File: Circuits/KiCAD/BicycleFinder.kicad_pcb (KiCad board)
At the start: 2 copper layers, 76.4 x 40.2 mm, 11 parts, among them P1 CONN_14, P2 CONN_14, P3 CONN_7, SW1 SW_PUSH, U1 LITE_LITE

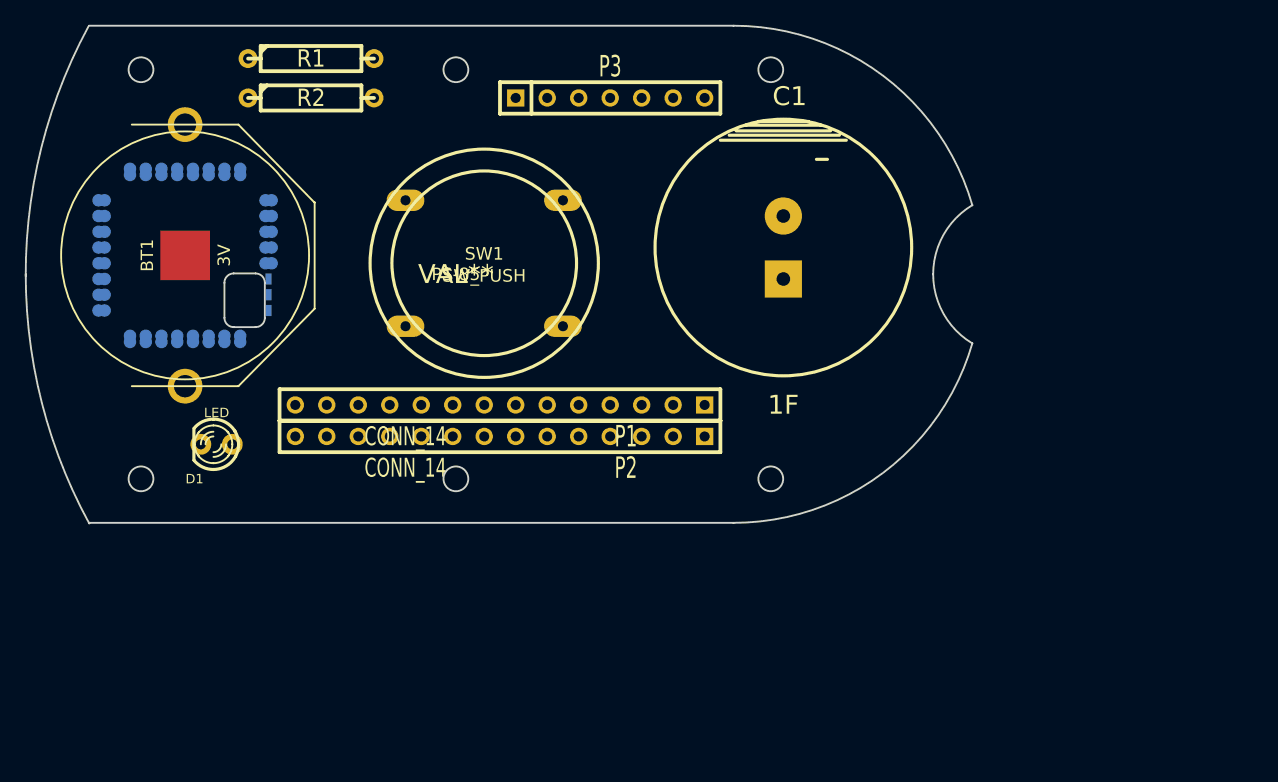
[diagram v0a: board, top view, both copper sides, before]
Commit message: Colored 1F EDLC.
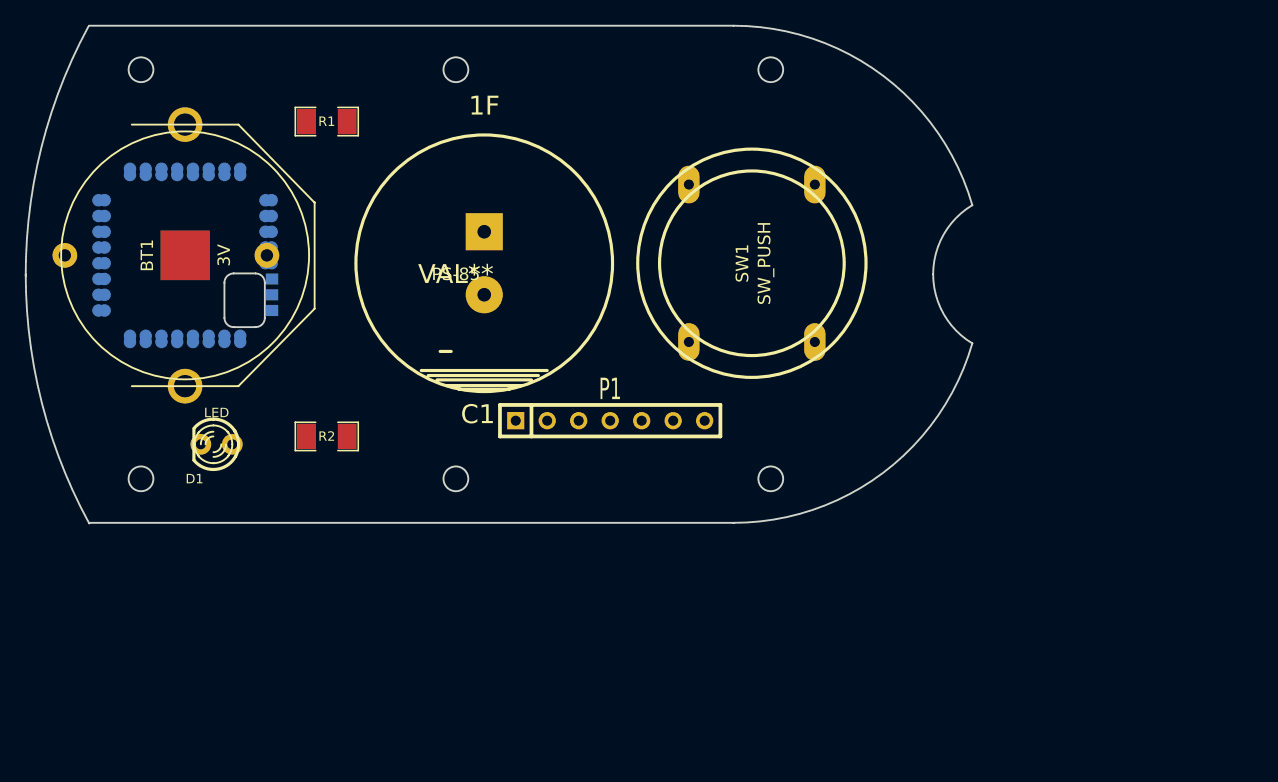
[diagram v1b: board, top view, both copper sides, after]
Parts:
- removed P2: CONN_14, SIL-14
- removed P3: CONN_7, SIL-7
- BT1: footprint BK-888 -> BK-888+BK-2032M
- P1: value CONN_14 -> CONN_7; footprint SIL-14 -> SIL-7
- R1, R2: value 1k -> 750; footprint R4 -> SM1206
- moved R2 27.3 mm to (36.8, 45.7)
- moved C1 24.2 mm to (49.5, 31.8), turned to 180 degrees
- moved SW1 21.6 mm to (71.1, 31.8), turned to 90 degrees
- moved P1 8.98 mm to (59.7, 44.5), turned to 0 degrees
- moved R1 5.24 mm to (36.8, 20.3)
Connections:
- C1 pad 1: /Vcc -> N-0000034
- D1 pad 2: /DO4 -> N-0000033
- P1 pad 1: GND -> N-0000034
- P1 pad 2: /SCL -> N-0000028
- P1 pad 3: /TXD -> N-0000029
- P1 pad 4: /PWM1 -> N-0000016
- P1 pad 5: /DO1 -> N-0000019
- P1 pad 6: /PWM2 -> N-0000028
- P1 pad 7: /PWM3 -> N-0000018
- R1 pad 2: /Vcc -> N-0000034
- R2 pad 2: /Vcc -> N-0000034
- SW1 pad 1: GND -> N-0000030
- SW1 pad 2: /DI1 -> GND
- U1 pad 1: /PWM2 -> (no net)
- U1 pad 10: /PWM4 -> (no net)
- U1 pad 11: /DO4 -> N-0000033
- U1 pad 12: /M1 -> N-0000018
- U1 pad 13: /DI1 -> N-0000030
- U1 pad 14: /SCL -> (no net)
- U1 pad 15: /DI2 -> (no net)
- U1 pad 16: /DI3 -> (no net)
- U1 pad 17: /SDA -> (no net)
- U1 pad 18: /DI4 -> (no net)
- U1 pad 19: /BPS -> (no net)
- U1 pad 2: /PWM3 -> N-0000016
- U1 pad 21: /RST -> N-0000028
- U1 pad 22: /AI3 -> (no net)
- U1 pad 23: /AI1 -> (no net)
- U1 pad 24: /AI2 -> (no net)
- U1 pad 25: /AI4 -> (no net)
- U1 pad 26: /M2 -> (no net)
- U1 pad 27: /M3 -> (no net)
- U1 pad 28: GND -> (no net)
- U1 pad 3: /DO1 -> (no net)
- U1 pad 4: /DO2 -> (no net)
- U1 pad 5: /Vcc -> N-0000034
- U1 pad 6: /DO3 -> (no net)
- U1 pad 7: /PWM1 -> (no net)
- U1 pad 8: /RXD -> N-0000029
- U1 pad 9: /TXD -> N-0000019

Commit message: Added 3D model of BK-888, BK-2032M, CR2032.
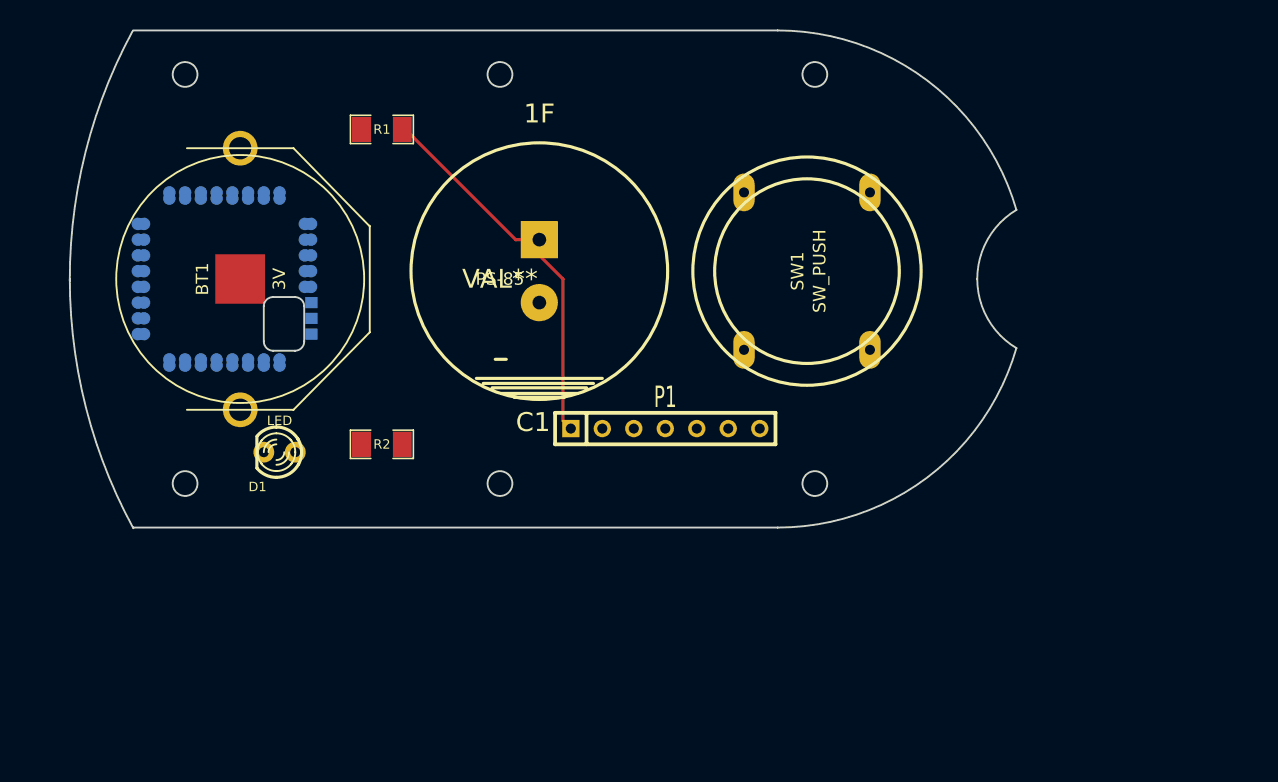
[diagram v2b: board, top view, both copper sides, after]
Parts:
- BT1: footprint BK-888+BK-2032M -> BK-888+CR2032
- moved D1 5.12 mm to (33.0, 47.0)
- moved BT1 4.84 mm to (29.8, 33.0)
- moved P1 4.49 mm to (64.1, 45.1)
- moved C1 4.49 mm to (54.0, 32.4)
- moved R1 4.49 mm to (41.3, 21.0)
- moved R2 4.49 mm to (41.3, 46.4)
- moved SW1 4.49 mm to (75.6, 32.4)
- moved U1 3.70 mm to (21.6, 40.0)
- moved PS-85 3.58 mm to (50.8, 33.0)
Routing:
- net N-0000034: track 0.00 -> 31.5 mm
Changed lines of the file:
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@@
 (kicad_pcb (version 3) (host pcbnew "(2013-07-07 BZR 4022)-stable")
   (general
-    (links 20)
-    (no_connects 20)
-    (area 12.214999 12.259999 92.573001 53.073059)
+    (links 18)
+    (no_connects 16)
+    (area 12.065 12.065 92.71 53.34)
     (thickness 1.6)
     (drawings 0)
-    (tracks 0)
+    (tracks 9)
     (zones 0)
     (modules 9)
@@
   )
   (module SW_PUSH-18mm   placed (layer F.Cu)
-    (at 71.12 31.75 90)
+    (at 75.565 32.385 90)
     (fp_text reference SW1 (at 0 -0.762 90) (layer F.SilkS)
       (effects (font (size 1.016 1.016) (thickness 0.2032)))
@@
   )
   (module LED-3MM (layer F.Cu)
-    (at 27.94 46.355 180)
+    (at 33.02 46.99 180)
     (descr "LED 3mm - Lead pitch 100mil (2,54mm)")
     (tags "LED led 3mm 3MM 100mil 2,54mm")
@@
   )
   (module PS-85 (layer F.Cu)
-    (at 47.244 32.639)
+    (at 50.8 33.02)
     (fp_text reference PS-85 (at 0 0) (layer F.SilkS)
       (effects (font (size 1 1) (thickness 0.15)))
@@
   )
   (module SE-5R5-D105VY   placed (layer F.Cu)
-    (at 49.53 31.75 180)
+    (at 53.975 32.385 180)
     (descr "Capacitor, EDLC, cyl 20.7x7.5mm")
     (fp_text reference C1 (at 0.508 -12.192 180) (layer F.SilkS)
@@
   )
   (module LITE (layer B.Cu)
-    (at 18.415 38.1 90)
+    (at 21.59 40.005 90)
     (fp_text reference U1 (at 0 0 90) (layer B.SilkS) hide
       (effects (font (size 0 0) (thickness 0.000001)) (justify mirror))
@@
   )
   (module SM1206 (layer F.Cu)
-    (at 36.83 20.32)
+    (at 41.275 20.955)
     (attr smd)
     (fp_text reference R1 (at 0 0) (layer F.SilkS)
@@
   )
   (module SM1206 (layer F.Cu)
-    (at 36.83 45.72)
+    (at 41.275 46.355)
     (attr smd)
     (fp_text reference R2 (at 0 0) (layer F.SilkS)
@@
   )
   (module SIL-7 (layer F.Cu)
-    (at 59.69 44.45)
+    (at 64.135 45.085)
     (descr "Connecteur 7 pins")
     (tags "CONN DEV")
@@
     )
   )
-  (module BK-888+BK-2032M (layer F.Cu)
-    (at 25.4 31.115 90)
+  (module BK-888+CR2032 (layer F.Cu)
+    (at 29.845 33.02 90)
     (fp_text reference BT1 (at 0 -3.05 90) (layer F.SilkS)
       (effects (font (size 1 1) (thickness 0.15)))
@@
     (fp_circle (center 0 0) (end 0 -10) (layer F.SilkS) (width 0.15))
     (pad 1 thru_hole circle (at -10.55 0 90) (size 2.8 2.8) (drill 1.8)
-      (layers *.Cu *.Mask F.SilkS)
+      (layers *.Mask B.Cu F.SilkS)
       (net 1 /3V)
     )
     (pad 1 thru_hole circle (at 10.55 0 90) (size 2.8 2.8) (drill 1.8)
-      (layers *.Cu *.Mask F.SilkS)
+      (layers *.Mask B.Cu F.SilkS)
       (net 1 /3V)
-    )
-    (pad 2 thru_hole circle (at 0 -9.7 90) (size 2 2) (drill 1)
-      (layers *.Cu *.Mask F.SilkS)
-      (net 2 GND)
-    )
-    (pad 2 thru_hole circle (at 0 6.6 90) (size 2 2) (drill 1)
-      (layers *.Cu *.Mask F.SilkS)
-      (net 2 GND)
     )
     (pad 2 smd rect (at 0 0 90) (size 4 4)
@@
       (net 2 GND)
     )
-  )
+    (model BK-888.wrl
+      (at (xyz 0 0 0))
+      (scale (xyz 0.393701 0.393701 0.393701))
+      (rotate (xyz 0 0 0))
+    )
+    (model CR2032.wrl
+      (at (xyz 0 0 0.009842999999999999))
+      (scale (xyz 0.393701 0.393701 0.393701))
+      (rotate (xyz 0 0 0))
+    )
+  )
+  (segment (start 42.926 46.355) (end 43.18 46.355) (width 0.254) (layer F.Cu) (net 11) (status 80000))
+  (segment (start 43.18 46.355) (end 42.926 46.355) (width 0.254) (layer F.Cu) (net 11) (status 80000))
+  (segment (start 53.975 29.845) (end 52.07 29.845) (width 0.254) (layer F.Cu) (net 11) (status 80000))
+  (segment (start 52.07 29.845) (end 43.18 20.955) (width 0.254) (layer F.Cu) (net 11) (status 80000))
+  (segment (start 43.18 20.955) (end 42.926 20.955) (width 0.254) (layer F.Cu) (net 11) (status 80000))
+  (segment (start 56.515 45.085) (end 55.88 44.45) (width 0.254) (layer F.Cu) (net 11) (status 80000))
+  (segment (start 55.88 44.45) (end 55.88 33.02) (width 0.254) (layer F.Cu) (net 11) (status 80000))
+  (segment (start 55.88 33.02) (end 53.975 31.115) (width 0.254) (layer F.Cu) (net 11) (status 80000))
+  (segment (start 53.975 31.115) (end 53.975 29.845) (width 0.254) (layer F.Cu) (net 11) (status 80000))
+  (zone (net 0) (net_name "") (layer F.Cu) (hatch edge 0.508)
+    (connect_pads (clearance 0.508))
+    (min_thickness 0.254)
+    (keepout (tracks not_allowed) (vias not_allowed) (copperpour allowed))
+    (fill (arc_segments 16) (thermal_gap 0.508) (thermal_bridge_width 0.508))
+    (polygon
+      (pts
+        (xy 35.56 40.005) (xy 21.59 40.005) (xy 21.59 26.035) (xy 35.56 26.035)
+      )
+    )
+  )

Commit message: Marked plus sign on BK-888 3D model.
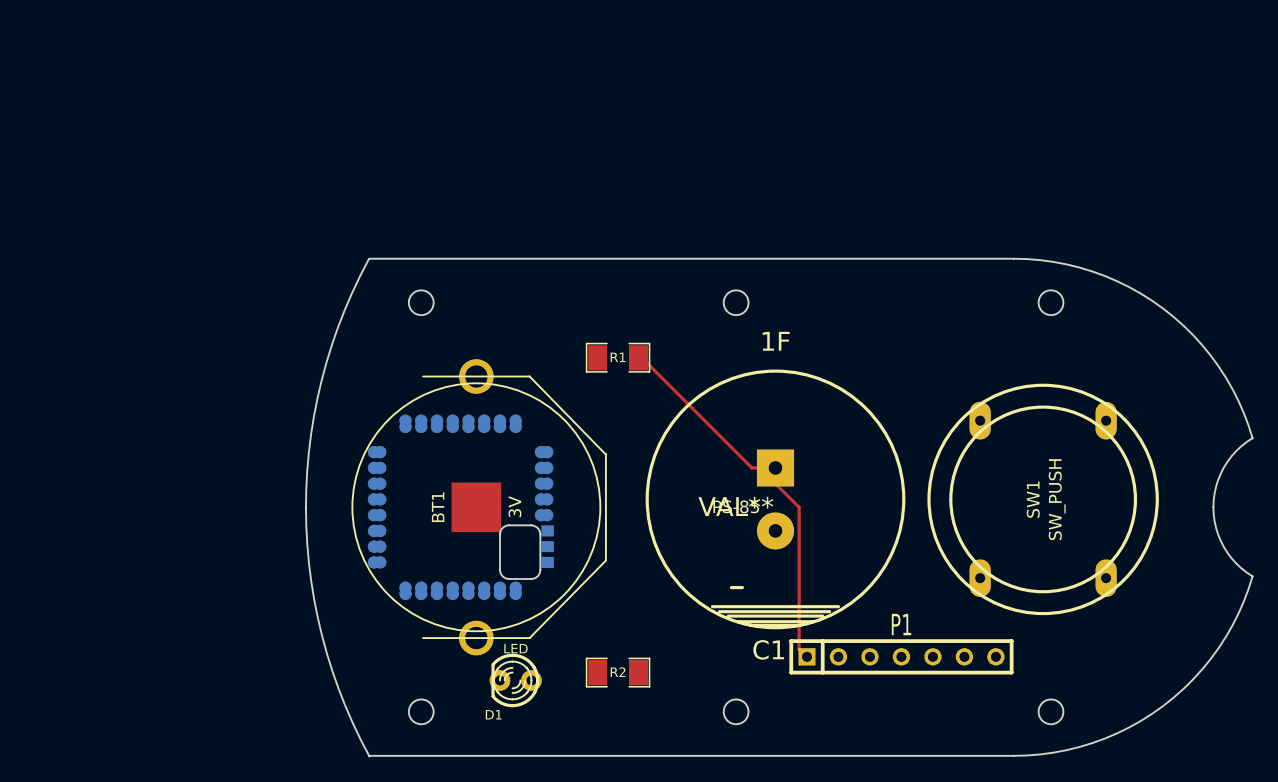
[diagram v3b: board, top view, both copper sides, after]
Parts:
- moved BT1 26.5 mm to (48.9, 51.4)
- moved C1 26.5 mm to (73.0, 50.8)
- moved R1 26.5 mm to (60.3, 39.4)
- moved R2 26.5 mm to (60.3, 64.8)
- moved D1 26.5 mm to (52.1, 65.4)
- moved P1 26.5 mm to (83.2, 63.5)
- moved PS-85 26.5 mm to (69.8, 51.4)
- moved SW1 26.5 mm to (94.6, 50.8)
- moved U1 26.5 mm to (40.6, 58.4)
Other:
- outline, holes or cut-outs redrawn
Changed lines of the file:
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@@
     (links 18)
     (no_connects 16)
-    (area 12.065 12.065 92.71 53.34)
+    (area 34.820999 31.055999 115.179001 71.869059)
     (thickness 1.6)
     (drawings 0)
@@
   )
   (module SW_PUSH-18mm   placed (layer F.Cu)
-    (at 75.565 32.385 90)
+    (at 94.615 50.8 90)
     (fp_text reference SW1 (at 0 -0.762 90) (layer F.SilkS)
       (effects (font (size 1.016 1.016) (thickness 0.2032)))
@@
   )
   (module LED-3MM (layer F.Cu)
-    (at 33.02 46.99 180)
+    (at 52.07 65.405 180)
     (descr "LED 3mm - Lead pitch 100mil (2,54mm)")
     (tags "LED led 3mm 3MM 100mil 2,54mm")
@@
   )
   (module PS-85 (layer F.Cu)
-    (at 50.8 33.02)
+    (at 69.85 51.435)
     (fp_text reference PS-85 (at 0 0) (layer F.SilkS)
       (effects (font (size 1 1) (thickness 0.15)))
@@
   )
   (module SE-5R5-D105VY   placed (layer F.Cu)
-    (at 53.975 32.385 180)
+    (at 73.025 50.8 180)
     (descr "Capacitor, EDLC, cyl 20.7x7.5mm")
     (fp_text reference C1 (at 0.508 -12.192 180) (layer F.SilkS)
@@
   )
   (module LITE (layer B.Cu)
-    (at 21.59 40.005 90)
+    (at 40.64 58.42 90)
     (fp_text reference U1 (at 0 0 90) (layer B.SilkS) hide
       (effects (font (size 0 0) (thickness 0.000001)) (justify mirror))
@@
   )
   (module SM1206 (layer F.Cu)
-    (at 41.275 20.955)
+    (at 60.325 39.37)
     (attr smd)
     (fp_text reference R1 (at 0 0) (layer F.SilkS)
@@
   )
   (module SM1206 (layer F.Cu)
-    (at 41.275 46.355)
+    (at 60.325 64.77)
     (attr smd)
     (fp_text reference R2 (at 0 0) (layer F.SilkS)
@@
   )
   (module SIL-7 (layer F.Cu)
-    (at 64.135 45.085)
+    (at 83.185 63.5)
     (descr "Connecteur 7 pins")
     (tags "CONN DEV")
@@
   )
   (module BK-888+CR2032 (layer F.Cu)
-    (at 29.845 33.02 90)
+    (at 48.895 51.435 90)
     (fp_text reference BT1 (at 0 -3.05 90) (layer F.SilkS)
       (effects (font (size 1 1) (thickness 0.15)))
@@
     )
   )
-  (segment (start 42.926 46.355) (end 43.18 46.355) (width 0.254) (layer F.Cu) (net 11) (status 80000))
-  (segment (start 43.18 46.355) (end 42.926 46.355) (width 0.254) (layer F.Cu) (net 11) (status 80000))
-  (segment (start 53.975 29.845) (end 52.07 29.845) (width 0.254) (layer F.Cu) (net 11) (status 80000))
-  (segment (start 52.07 29.845) (end 43.18 20.955) (width 0.254) (layer F.Cu) (net 11) (status 80000))
-  (segment (start 43.18 20.955) (end 42.926 20.955) (width 0.254) (layer F.Cu) (net 11) (status 80000))
-  (segment (start 56.515 45.085) (end 55.88 44.45) (width 0.254) (layer F.Cu) (net 11) (status 80000))
-  (segment (start 55.88 44.45) (end 55.88 33.02) (width 0.254) (layer F.Cu) (net 11) (status 80000))
-  (segment (start 55.88 33.02) (end 53.975 31.115) (width 0.254) (layer F.Cu) (net 11) (status 80000))
-  (segment (start 53.975 31.115) (end 53.975 29.845) (width 0.254) (layer F.Cu) (net 11) (status 80000))
+  (segment (start 61.976 64.77) (end 62.23 64.77) (width 0.254) (layer F.Cu) (net 11) (status 80000))
+  (segment (start 62.23 64.77) (end 61.976 64.77) (width 0.254) (layer F.Cu) (net 11) (status 80000))
+  (segment (start 73.025 48.26) (end 71.12 48.26) (width 0.254) (layer F.Cu) (net 11) (status 80000))
+  (segment (start 71.12 48.26) (end 62.23 39.37) (width 0.254) (layer F.Cu) (net 11) (status 80000))
+  (segment (start 62.23 39.37) (end 61.976 39.37) (width 0.254) (layer F.Cu) (net 11) (status 80000))
+  (segment (start 75.565 63.5) (end 74.93 62.865) (width 0.254) (layer F.Cu) (net 11) (status 80000))
+  (segment (start 74.93 62.865) (end 74.93 51.435) (width 0.254) (layer F.Cu) (net 11) (status 80000))
+  (segment (start 74.93 51.435) (end 73.025 49.53) (width 0.254) (layer F.Cu) (net 11) (status 80000))
+  (segment (start 73.025 49.53) (end 73.025 48.26) (width 0.254) (layer F.Cu) (net 11) (status 80000))
   (zone (net 0) (net_name "") (layer F.Cu) (hatch edge 0.508)
     (connect_pads (clearance 0.508))
@@
     (polygon
       (pts
-        (xy 35.56 40.005) (xy 21.59 40.005) (xy 21.59 26.035) (xy 35.56 26.035)
+        (xy 54.61 58.42) (xy 40.64 58.42) (xy 40.64 44.45) (xy 54.61 44.45)
       )
     )

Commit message: Swapped location of bigger parts.
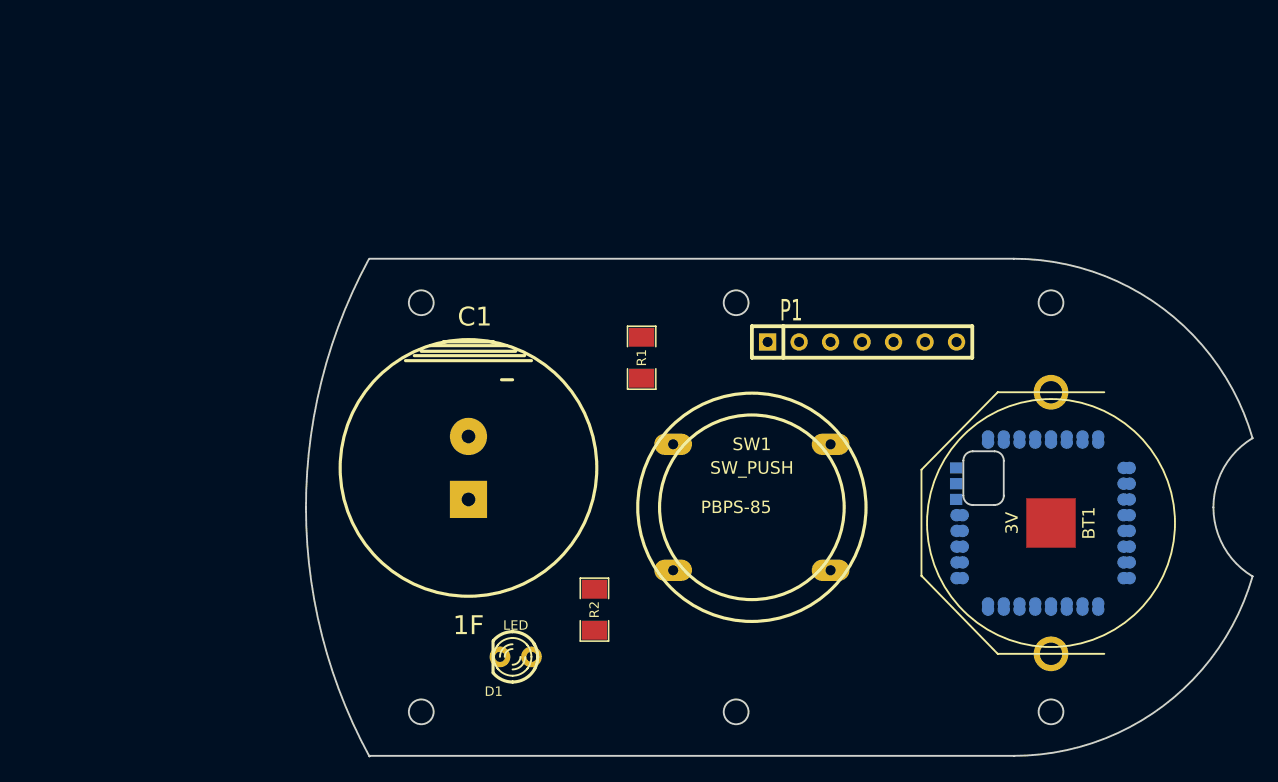
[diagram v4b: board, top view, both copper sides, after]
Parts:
- PBPS-85: renamed from PS-85; value VAL** -> (none)
- SW1: footprint SW_PUSH-18mm -> JF-15CKCBNP2
- moved U1 62.3 mm to (101.6, 45.7), turned to 270 degrees
- moved BT1 46.4 mm to (95.2, 52.7), turned to 270 degrees
- moved P1 25.6 mm to (80.0, 38.1)
- moved C1 24.9 mm to (48.3, 48.3), turned to 0 degrees
- moved SW1 23.5 mm to (71.1, 51.4), turned to 180 degrees
- moved R2 5.43 mm to (58.4, 59.7), turned to 90 degrees
- moved D1 1.91 mm to (52.1, 63.5)
- moved R1 1.90 mm to (62.2, 39.4), turned to 90 degrees
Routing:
- net N-0000034: track 31.5 -> 0.00 mm

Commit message: Moved P1 to keep distance from NTH.
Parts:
- moved P1 3.17 mm to (83.2, 38.1)
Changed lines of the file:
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@@
   )
   (module SIL-7 (layer F.Cu)
-    (at 80.01 38.1)
+    (at 83.185 38.1)
     (descr "Connecteur 7 pins")
     (tags "CONN DEV")
